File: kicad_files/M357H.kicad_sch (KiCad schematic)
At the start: 55 parts, among them J1 SM04B-SRSS-TB(LF)(SN), Q1 2N7002, Q2 2N7002, SW1 K2-1187SQ-A4SW-06, U1 STM32F401-LQFP64, U90 TXS0101DCKR, X1 EXTRA_PINS, X2 Conn_02x04_Odd_Even, X3 ARM JTAG, Y1 25MHz

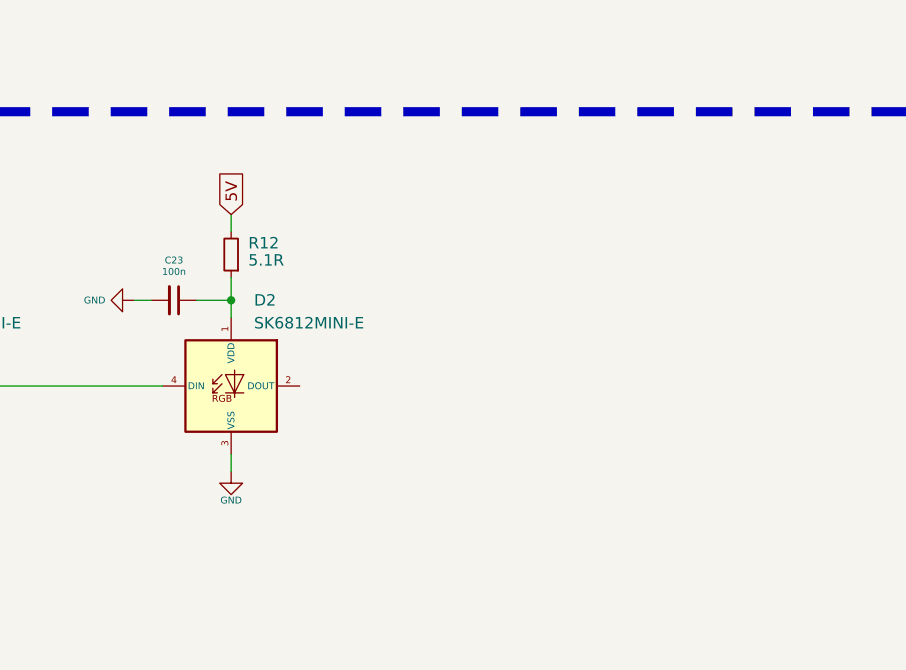
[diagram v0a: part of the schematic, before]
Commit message: Add fourth indicator
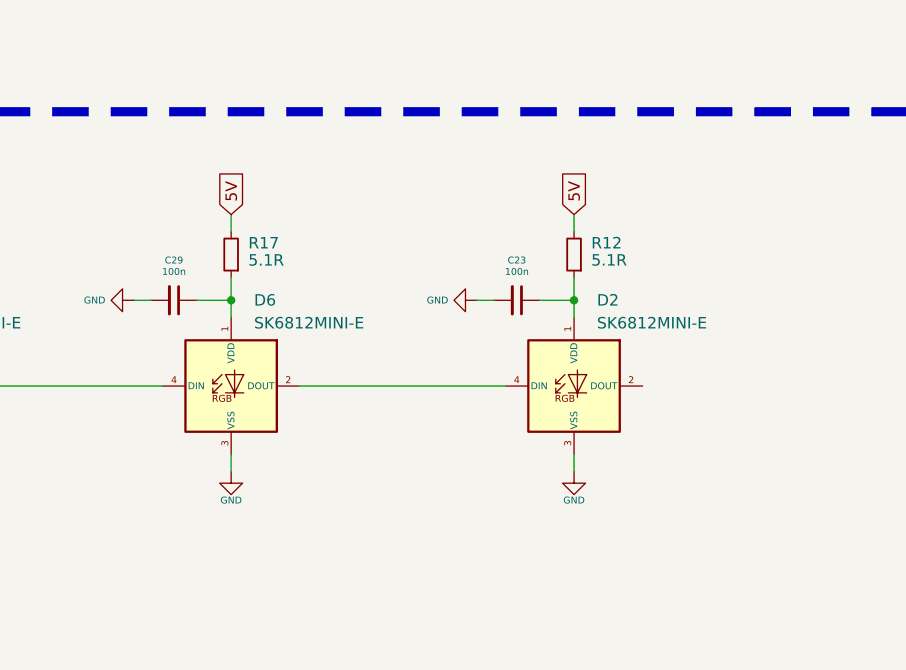
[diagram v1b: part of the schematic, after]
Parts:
- added C29: 100n, Capacitor_SMD:C_0402_1005Metric, symbol Device:C_Small
- added D6: SK6812MINI-E, acheron_Components:SK6812MINI_3535_6028_3.2x2.8mm_Round, symbol acheronSymbols:SK6812MINI-E
- added R17: 5.1R, Resistor_SMD:R_0402_1005Metric, symbol Device:R_Small
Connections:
- net 5V: now also R17.2
- net GND: now also C29.2, D6.3 (VSS)
- net at D2.4 (DIN): now also D6.2 (DOUT); no longer D5.2 (DOUT)
- new net: C29.1, D6.1 (VDD), R17.1
- new net: D5.2 (DOUT), D6.4 (DIN)
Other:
- moved on the sheet: C23, D2, R12

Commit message: Pre-release modifications and checks
- Organize schematic, designators reset
- Remove empty "opamps" sheet
- Finish routing
- DRC ran, errors corrected
- Indicator cutout smoothened
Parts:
- X2: value Conn_02x04_Odd_Even -> EXTRA_PINS
- renumbered C3 to C1, C12 to C10, C1 to C11, C2 to C12, C24 to C13, C25 to C14, C26 to C15, C27 to C16, C28 to C17, C29 to C18, C23 to C19, C4 to C2, C5 to C3, C6 to C4, C7 to C5, C8 to C6, C9 to C7, C10 to C8, C11 to C9, D3 to D2, D4 to D3, D5 to D4, D6 to D5, D2 to D6, R8 to R1, R9 to R10, R14 to R11, R15 to R12, R16 to R13, R17 to R14, R12 to R15, R13 to R16, R10 to R2, R1 to R3, R2 to R4, R3 to R5, R4 to R6, R5 to R7, R6 to R8, R7 to R9, U90 to U2
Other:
- removed sheet OPAMPS
- note added: "ARR GEE BEE"
- note removed: "Recommended circuit in [1], except for 100R."
- moved on the sheet: C1, C10, C11, C12, C13, C14, C15, C16, C17, C18, C19, C2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

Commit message: Update some components metadata up to RGB LEDs
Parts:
- C1, C10, C2, C3, C8: Manufacturer Kyocera -> Guangdong Fenghua Advanced Tech
- C4, C5: Manufacturer Part Number 0402CG150J500NT -> 0603B103K500NT; Vendor Part Number LCSC C1548 -> LCSC C57112
- C6: Manufacturer Kyocera -> Samsung; Manufacturer Part Number 06035C104KAT2A -> CL10A475KO8NNNC; Vendor Part Number LCSC C88476 -> LCSC C19666
- C9: Manufacturer (none) -> Samsung; Manufacturer Part Number (none) -> CL10A475KO8NNNC; Vendor Part Number (none) -> LCSC C19666
- D2, D3, D4, D5, D6: Manufacturer (none) -> OPSCO; Manufacturer Part Number (none) -> SK6812MINI-E; PKG 3228 -> (none); Vendor Part Number (none) -> LCSC C5149201
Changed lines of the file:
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@@
 			)
 		)
-		(property "Manufacturer" "Kyocera"
+		(property "Manufacturer" "Guangdong Fenghua Advanced Tech"
 			(at 133.35 50.8 0)
 			(effects
@@
 			)
 		)
-		(property "PKG" "3228"
+		(property "PKG" ""
 			(at 267.335 289.0198 0)
 			(effects
@@
 			)
 		)
+		(property "Manufacturer" "OPSCO"
+			(at 254 292.1 0)
+			(effects
+				(font
+					(size 1.27 1.27)
+				)
+				(hide yes)
+			)
+		)
+		(property "Manufacturer Part Number" "SK6812MINI-E"
+			(at 254 292.1 0)
+			(effects
+				(font
+					(size 1.27 1.27)
+				)
+				(hide yes)
+			)
+		)
+		(property "Vendor Part Number" "LCSC C5149201"
+			(at 254 292.1 0)
+			(effects
+				(font
+					(size 1.27 1.27)
+				)
+				(hide yes)
+			)
+		)
 		(pin "1"
 		)
@@
 			)
 		)
-		(property "Manufacturer" "Kyocera"
+		(property "Manufacturer" "Guangdong Fenghua Advanced Tech"
 			(at 146.05 193.675 0)
 			(effects
@@
 			)
 		)
-		(property "Manufacturer" "Kyocera"
+		(property "Manufacturer" "Samsung"
 			(at 101.6 149.225 0)
 			(effects
@@
 			)
 		)
-		(property "Manufacturer Part Number" "06035C104KAT2A"
+		(property "Manufacturer Part Number" "CL10A475KO8NNNC"
 			(at 101.6 149.225 0)
 			(effects
@@
 			)
 		)
-		(property "Vendor Part Number" "LCSC C88476"
+		(property "Vendor Part Number" "LCSC C19666"
 			(at 101.6 149.225 0)
 			(effects
@@
 			)
 		)
-		(property "Manufacturer" "Kyocera"
+		(property "Manufacturer" "Guangdong Fenghua Advanced Tech"
 			(at 266.7 73.025 0)
 			(effects
@@
 			)
 		)
-		(property "Manufacturer" ""
+		(property "Manufacturer" "Samsung"
 			(at 225.425 180.975 0)
 			(effects
@@
 			)
 		)
-		(property "Manufacturer Part Number" ""
+		(property "Manufacturer Part Number" "CL10A475KO8NNNC"
 			(at 225.425 180.975 0)
 			(effects
@@
 			)
 		)
-		(property "Vendor Part Number" ""
+		(property "Vendor Part Number" "LCSC C19666"
 			(at 225.425 180.975 0)
 			(effects
@@
 			)
 		)
-		(property "Manufacturer" "Kyocera"
+		(property "Manufacturer" "Guangdong Fenghua Advanced Tech"
 			(at 247.65 174.625 0)
 			(effects
@@
 			)
 		)
-		(property "PKG" "3228"
+		(property "PKG" ""
 			(at 191.135 289.0198 0)
 			(effects
@@
 			)
 		)
+		(property "Manufacturer" "OPSCO"
+			(at 177.8 292.1 0)
+			(effects
+				(font
+					(size 1.27 1.27)
+				)
+				(hide yes)
+			)
+		)
+		(property "Manufacturer Part Number" "SK6812MINI-E"
+			(at 177.8 292.1 0)
+			(effects
+				(font
+					(size 1.27 1.27)
+				)
+				(hide yes)
+			)
+		)
+		(property "Vendor Part Number" "LCSC C5149201"
+			(at 177.8 292.1 0)
+			(effects
+				(font
+					(size 1.27 1.27)
+				)
+				(hide yes)
+			)
+		)
 		(pin "1"
 		)
@@
 			)
 		)
-		(property "PKG" "3228"
+		(property "PKG" ""
 			(at 305.435 289.0198 0)
 			(effects
@@
 			)
 		)
+		(property "Manufacturer" "OPSCO"
+			(at 292.1 292.1 0)
+			(effects
+				(font
+					(size 1.27 1.27)
+				)
+				(hide yes)
+			)
+		)
+		(property "Manufacturer Part Number" "SK6812MINI-E"
+			(at 292.1 292.1 0)
+			(effects
+				(font
+					(size 1.27 1.27)
+				)
+				(hide yes)
+			)
+		)
+		(property "Vendor Part Number" "LCSC C5149201"
+			(at 292.1 292.1 0)
+			(effects
+				(font
+					(size 1.27 1.27)
+				)
+				(hide yes)
+			)
+		)
 		(pin "1"
 		)
@@
 			)
 		)
-		(property "PKG" "3228"
+		(property "PKG" ""
 			(at 153.035 289.0198 0)
 			(effects
@@
 			)
 		)
+		(property "Manufacturer" "OPSCO"
+			(at 139.7 292.1 0)
+			(effects
+				(font
+					(size 1.27 1.27)
+				)
+				(hide yes)
+			)
+		)
+		(property "Manufacturer Part Number" "SK6812MINI-E"
+			(at 139.7 292.1 0)
+			(effects
+				(font
+					(size 1.27 1.27)
+				)
+				(hide yes)
+			)
+		)
+		(property "Vendor Part Number" "LCSC C5149201"
+			(at 139.7 292.1 0)
+			(effects
+				(font
+					(size 1.27 1.27)
+				)
+				(hide yes)
+			)
+		)
 		(pin "1"
 		)
@@
 			)
 		)
-		(property "Manufacturer Part Number" "0402CG150J500NT"
+		(property "Manufacturer Part Number" "0603B103K500NT"
 			(at 44.45 135.255 0)
 			(effects
@@
 			)
 		)
-		(property "Vendor Part Number" "LCSC C1548"
+		(property "Vendor Part Number" "LCSC C57112"
 			(at 44.45 135.255 0)
 			(effects
@@
 			)
 		)
-		(property "Manufacturer" "Kyocera"
+		(property "Manufacturer" "Guangdong Fenghua Advanced Tech"
 			(at 120.65 73.025 0)
 			(effects
@@
 			)
 		)
-		(property "Manufacturer Part Number" "0402CG150J500NT"
+		(property "Manufacturer Part Number" "0603B103K500NT"
 			(at 57.15 135.255 0)
 			(effects
@@
 			)
 		)
-		(property "Vendor Part Number" "LCSC C1548"
+		(property "Vendor Part Number" "LCSC C57112"
 			(at 57.15 135.255 0)
 			(effects
@@
 			)
 		)
-		(property "PKG" "3228"
+		(property "PKG" ""
 			(at 229.235 289.0198 0)
 			(effects
 				(font
+					(size 1.27 1.27)
+				)
+				(hide yes)
+			)
+		)
+		(property "Manufacturer" "OPSCO"
+			(at 215.9 292.1 0)
+			(effects
+				(font
+					(size 1.27 1.27)
+				)
+				(hide yes)
+			)
+		)
+		(property "Manufacturer Part Number" "SK6812MINI-E"
+			(at 215.9 292.1 0)
+			(effects
+				(font
+					(size 1.27 1.27)
+				)
+				(hide yes)
+			)
+		)
+		(property "Vendor Part Number" "LCSC C5149201"
+			(at 215.9 292.1 0)
+			(effects
+				(font

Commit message: Finish adding metadata, release-ready
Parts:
- C4: Manufacturer Part Number 0603B103K500NT -> 0402CG200J500NT; Vendor Part Number LCSC C57112 -> LCSC C1554
- C5: Manufacturer Part Number 0603B103K500NT -> 0402CG200J500NT; Specification 50V 15pF C0G ±5% 0402 MLCC -> 50V 20pF C0G ±5% 0402 MLCC; Vendor Part Number LCSC C57112 -> LCSC C1554
- H1, H2, H3, H4: Vendor Part Number (none) -> LCSC 732-7088-
- J1: LCSC Part Number C160404 -> (none); Vendor Part Number (none) -> LCSC C160404
- R1: Manufacturer (none) -> Uniroyal; Manufacturer Part Number (none) -> 0603WAF0000T5E; Vendor Part Number (none) -> LCSC C21189
- R2: Manufacturer FOJAN -> Uniroyal; Manufacturer Part Number FRC0603F1000TS -> 0603WAF1004T5E; Vendor Part Number LCSC C2906981 -> LCSC C22935
- U1: value STM32F401-LQFP64 -> STM32F401RCT6; Manufacturer (none) -> STMicroelectronics; Manufacturer Part Number (none) -> STM32F401RCT6; Vendor Part Number (none) -> LCSC C74524
- X1, X2: now left out of the parts list
- Y1: value 25MHz -> TAXM8M4RFDCET2T; Manufacturer (none) -> TAE; Manufacturer Part Number (none) -> TAXM8M4RFDCET2T; Package (none) -> Y3225_4P; Specification (none) -> 8MHz 3225-4P oscillator crystal; Vendor Part Number (none) -> LCSC C403948
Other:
- moved on the sheet: GR1, GR2, GR3, H1, H2, H3, H4, J1
